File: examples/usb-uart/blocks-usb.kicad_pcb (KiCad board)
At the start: 2 copper layers, 31 x 29 mm, 13 parts, among them U1 ESD 2-line, U2 LDO 3.3V 300mA, U3 USB-UART

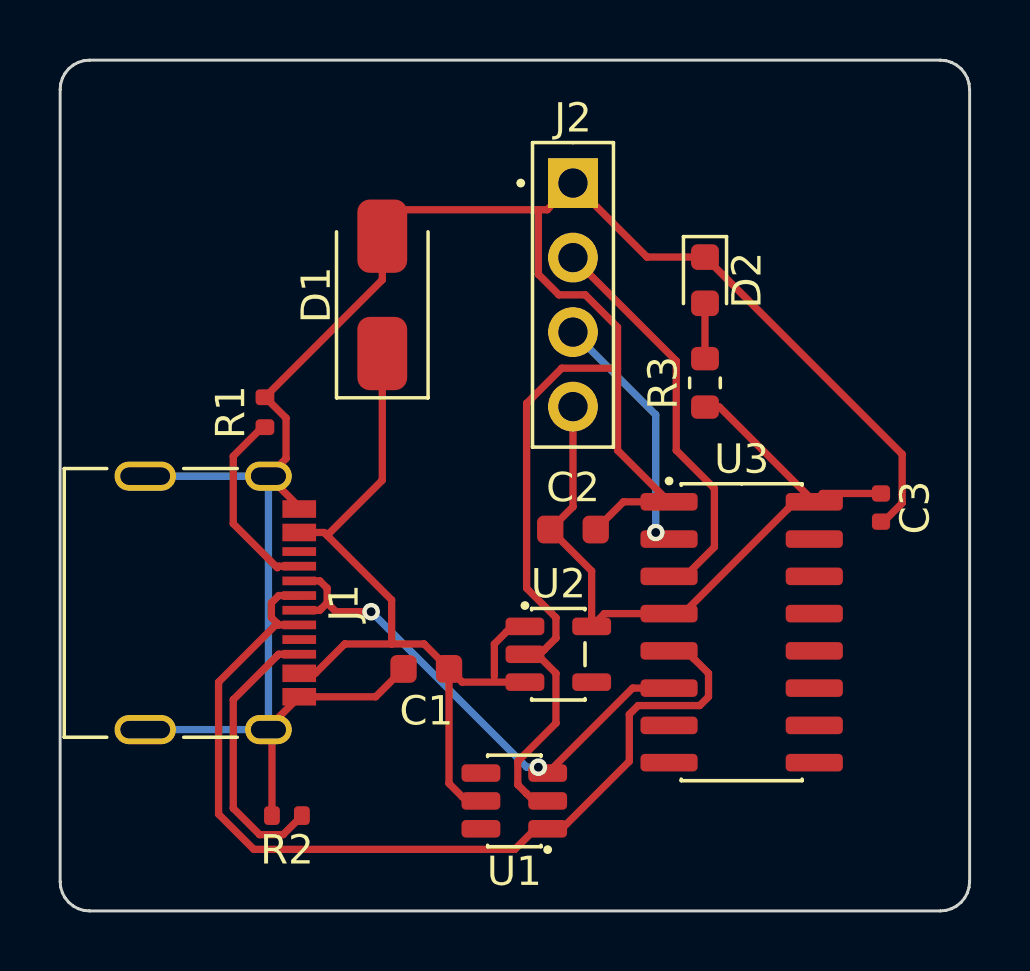
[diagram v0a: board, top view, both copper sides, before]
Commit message: doom, examples: re-route around the USB-C receptacle's new land pattern
The standard receptacle became GCT USB4105's recommended layout (pcbkit 7e43c086): its shield
legs moved and two unplated guide holes appeared, under the copper these boards had been routed
with (solder-mask-bridge and clearance errors at J1). `build.run` re-routed the 3–5 nets that
crossed it: all seven check complete with 0 errors again; the six Doom boards export for the fab
without --force.

Claude-Session: https://claude.ai/code/session_01GffCzZXi9ShujPbky1eccg
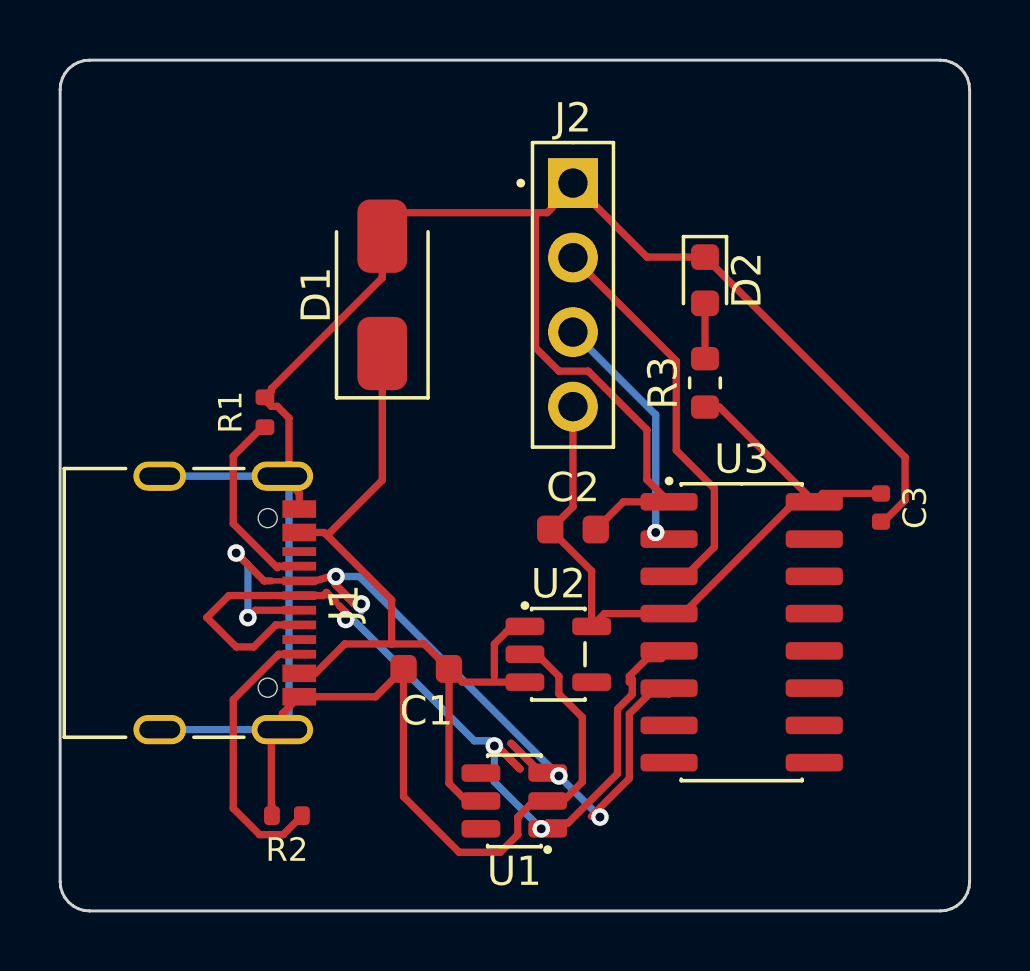
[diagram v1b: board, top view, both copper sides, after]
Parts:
- J1: value (none) -> USB4105-GF-A
- U1: value ESD 2-line -> USBLC6-2SC6
- U2: value LDO 3.3V 300mA -> AP2112K-3.3TRG1
- U3: value USB-UART -> CH340C
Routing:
- net DN: track 17.5 -> 32.2 mm, vias 2 -> 6
- net GND: track 95.5 -> 93.4 mm
- net DP: track 32.7 -> 30.9 mm, vias 0 -> 3

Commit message: boards: 15 boards rebuilt on pcbkit 20ffacdc9 (their pours under the 0.25 mm hole clearance)
Every board checked with main: 17 of 44 failed on hole-clearance (pours filled before fill c6 made
0.25 mm KiCad's hole clearance the default), keepout (holes now sized by the board) or
place-corner. design.run {} on each (placement and routing kept, pours refilled): 15 now complete,
0 errors. Not here: esp32-p4-touch-lcd-7b and p4-touch-7 (a build reroutes their pairs: 21 and 7
unrouted; kept as they were, 2,372 and 919 hole-clearance errors: a refill without a reroute is
needed).

Claude-Session: https://claude.ai/code/session_01BAgp959tApA8aEg85EYgfb
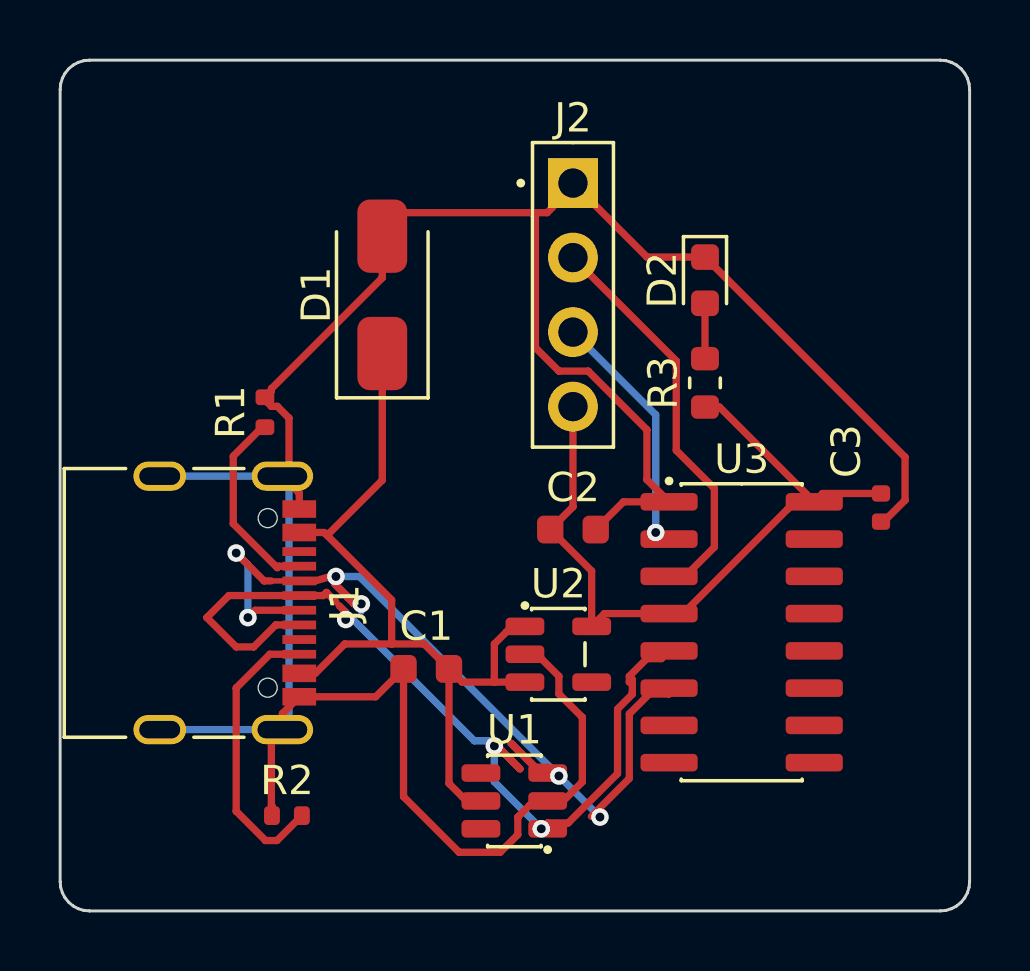
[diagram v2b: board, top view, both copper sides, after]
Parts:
- J2: value (none) -> PinHeader_1x04_P2.54mm_Vertical
